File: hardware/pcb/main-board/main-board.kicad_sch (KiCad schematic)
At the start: 44 parts, among them J1 USB-C, J10 CH552G_KEYBOARD_MCU, J11 KEYBOARD_BACKLIGHT_LEDS, J12 SPEAKER_1W_8OHM, J2 BATT_2x18650_PARALLEL, J3 BOOT0_OVERRIDE_JUMPER, J4 SWD_DEBUG, J5 MICROSD, J6 CR2032_HOLDER, J7 U.FL, J8 SMA_EDGE, J9 RA8875_DISPLAY_MODULE, Q1 2N7002, SW1 PWR_KEY, SW2 RESET, U1 MCP73831-2-OT, U10 PAM8403D, U2 IP5306, U3 AMS1117-3.3, U4 AMS1117-3.3, U5 GD32VF103CCT6, U6 W25Q64JVSSIQ, U7 23LC1024, U8 DS3231M, U9 ESP32-C3-MINI-1U, Y1 8MHz

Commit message: hardware: add PCB component placement for the Main Board
Adds main-board.kicad_pcb: every part from the schematic placed within
the 100x80mm board outline (hardware/bom.md's Board 2 spec), on the
correct nets (full ratsnest), courtyard-overlap/shorting/clearance clean
per kicad-cli pcb drc. No copper routing yet -- that's manual follow-on
work in the KiCad GUI (no autorouter available here).

Placement (kicad_gen/build_pcb.py) is computed from each footprint's real
measured courtyard geometry via pcbnew, not guessed -- a first hand-placed
attempt produced 7 courtyard overlaps once real sizes were checked (the
CR2032 holder alone is 27x24mm). Also fixes a footprint-anchor bug found
along the way: schematic instances without an explicit footprint override
were emitting an empty Footprint property, silently blanking out several
real KiCad-library defaults, which in turn exposed three wrong footprint
references (CR2032 holder was pointing at a 9V PP3 clip; two RF connectors
used a nonexistent library name).

Also fixes a schematic-legibility bug: net labels for left-pointing pins
grew back into the component body instead of away from it, and several
component Value fields held long descriptive sentences that collided with
neighboring text -- both cleaned up, with the descriptive notes moved to
README.md instead.

Co-Authored-By: Claude Sonnet 5 <noreply@anthropic.com>
Claude-Session: https://claude.ai/code/session_01Qv22nN2Gzvn3yFBup6Askg
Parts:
- C1, C2, C3: footprint (none) -> Capacitor_SMD:C_0603_1608Metric
- D1, D2: footprint (none) -> LED_SMD:LED_0603_1608Metric
- J5: footprint Connector_Card:Molex_502031-0810_MicroSD -> Connector_Card:microSD_HC_Molex_104031-0811
- J6: footprint Battery:BatteryHolder_MPD_BA9V-1_1x20mm -> Battery:BatteryHolder_MYOUNG_BS-07-A1BJ001_CR2032
- J7: footprint RF_Connector:U.FL_Molex_MCRF_73412-0110 -> Connector_Coaxial:U.FL_Molex_MCRF_73412-0110_Vertical
- Q1: footprint (none) -> Package_TO_SOT_SMD:SOT-23
- R1, R10, R11, R12, R13, R2, R3, R4, R5, R6, R7, R8, R9: footprint (none) -> Resistor_SMD:R_0603_1608Metric
- SW1, SW2: footprint (none) -> Button_Switch_THT:SW_PUSH_6mm_H4.3mm
- U1: footprint (none) -> Package_TO_SOT_SMD:SOT-23-5
- U10: footprint (none) -> Package_SO:SOP-16_3.9x9.9mm_P1.27mm
- U2: footprint (none) -> Package_SO:SOP-8_3.9x4.9mm_P1.27mm
- U3, U4: footprint (none) -> Package_TO_SOT_SMD:SOT-223-3_TabPin2
- U5: footprint (none) -> Package_QFP:LQFP-48_7x7mm_P0.5mm
- U6: footprint (none) -> Package_SO:SOIC-8_5.3x5.3mm_P1.27mm
- U7: footprint (none) -> Package_SO:SOIC-8_3.9x4.9mm_P1.27mm
- U8: footprint (none) -> Package_SO:SOIC-16W_7.5x10.3mm_P1.27mm
- U9: footprint (none) -> RF_Module:ESP32-C3-WROOM-02U
- Y1: footprint (none) -> Crystal:Crystal_SMD_HC49-SD

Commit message: hardware: fix real pin-number bugs found by datasheet verification
Checked all four custom part symbols (23LC1024, GD32VF103CCT6,
ESP32-C3-MINI-1U, IP5306) against their primary-source datasheets.
23LC1024 was already correct. The other three were substantially
wrong, not just unverified:

- GD32VF103CCT6: 35 of 48 pins (14-48) numbered wrong -- two spurious
  power-pin insertions shifted everything after them.
- ESP32-C3-MINI-1U: the symbol numbered its 19 signal pins 1-19
  sequentially; the real 53-pad module has GND/NC scattered through
  that range, so almost nothing lined up.
- IP5306: all 8 pins wrong, plus LED3 and SW (the boost converter's
  inductor node) were missing entirely, and two GND pins were invented
  that don't exist -- the real part's only ground is the PowerPAD.
  Fixing this surfaced a real design gap: no inductor exists anywhere
  in this design, so the boost path can't function yet.

Re-mapped every schematic net/power/no_connect reference to these
three parts to the corrected pin numbers and regenerated the
schematic -- ERC clean (320 warnings, 0 errors, same benign categories
as before).

main-board.kicad_pcb is deliberately left untouched: it was routed
against the old (wrong) netlist, so its net-to-pad assignments on all
three parts are now wrong, not just stale. Documented this plainly in
the PCB README rather than silently leaving a fabrication-unsafe board
looking finished.

Co-Authored-By: Claude Sonnet 5 <noreply@anthropic.com>
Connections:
- net +3V3_MCU: now also U5.24 (VDD_1), U5.36 (VDD_2), U5.48 (VDD_3); no longer U5.15 (VDD_1), U5.26 (VDD_2), U5.38 (VDD_3)
- net +3V3_RF: now also U9.3 (3V3); no longer U9.2 (3V3)
- net +5V: now also U2.8 (VOUT); no longer U2.5 (VOUT)
- net AUDIO_PWM: now also U5.14 (PA4); no longer U5.16 (PA4)
- net AUDIO_SHDN: now also U5.29 (PA8); no longer U5.31 (PA8)
- net BATT_LED1: now also U2.2 (LED1); no longer U2.7 (LED1)
- net BOOT0: now also U5.44 (BOOT0); no longer U5.46 (BOOT0)
- net BOOT1: now also U5.20 (PB2/BOOT1); no longer U5.22 (PB2/BOOT1)
- net DISP_CS: now also U5.25 (PB12); no longer U5.27 (PB12)
- net DISP_RESET: now also U5.38 (PA15); no longer U5.40 (PA15)
- net ESP_EN: now also U9.8 (EN); no longer U9.3 (EN)
- net ESP_IO9: now also U9.23 (IO9/BOOT); no longer U9.13 (IO9/BOOT)
- net GND: now also U2.9 (GND), U5.23 (VSS_1), U5.35 (VSS_2), U5.47 (VSS_3), U9.2 (GND); no longer U2.3 (GND), U2.6 (GND), U5.14 (VSS_1), U5.25 (VSS_2), U5.37 (VSS_3), U9.19 (GND)
- net I2C1_SCL: now also U5.42 (PB6); no longer U5.44 (PB6)
- net I2C1_SDA: now also U5.43 (PB7); no longer U5.45 (PB7)
- net KBD_BACKLIGHT_PWM: now also U5.41 (PB5); no longer U5.43 (PB5)
- net PWR_KEY: now also U2.5 (KEY); no longer U2.4 (KEY)
- net SPI1_MISO: now also U5.16 (PA6); no longer U5.18 (PA6)
- net SPI1_MOSI: now also U5.17 (PA7); no longer U5.19 (PA7)
- net SPI1_SCK: now also U5.15 (PA5); no longer U5.17 (PA5)
- net SPI2_MISO: now also U5.27 (PB14); no longer U5.29 (PB14)
- net SPI2_MOSI: now also U5.28 (PB15); no longer U5.30 (PB15)
- net SPI2_SCK: now also U5.26 (PB13); no longer U5.28 (PB13)
- net SWCLK: now also U5.37 (PA14/SWCLK); no longer U5.39 (PA14/SWCLK)
- net SWDIO: now also U5.34 (PA13/SWDIO); no longer U5.36 (PA13/SWDIO)
- net USART1_RX: now also U5.31 (PA10), U9.31 (U0TXD); no longer U5.33 (PA10), U9.18 (U0TXD)
- net USART1_TX: now also U5.30 (PA9), U9.30 (U0RXD); no longer U5.32 (PA9), U9.17 (U0RXD)
- net USART2_RX: now also U5.40 (PB4); no longer U5.42 (PB4)
- net USART2_TX: now also U5.39 (PB3); no longer U5.41 (PB3)
- net USB_DN: now also U9.26 (IO18/USB_D-); no longer U9.15 (IO18/USB_D-)
- net USB_DP: now also U9.27 (IO19/USB_D+); no longer U9.16 (IO19/USB_D+)
- net VBATT: now also U2.6 (BAT); no longer U2.2 (BAT)
- no-connect marks 31 -> 33

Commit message: hardware: add the IP5306's missing boost inductor
Datasheet verification (previous commit) found the IP5306's SW pin
(the boost converter's switch node) was wired to nothing -- the boost
path (BAT -> VOUT) couldn't function without an inductor there, and
none existed anywhere in this design.

Fixed per the IP5306 datasheet's own "Typical Application Schematic"
(Figure 7): a 1uH inductor (L1) bridges SW to BAT directly, not to
VOUT as an earlier read of this design assumed -- it's shared between
the buck charger and boost discharger. Added the reference circuit's
RC snubber (R14 0.5R + C4 22uF) on the SW node and a VOUT decoupling
cap (C5, simplified from the datasheet's 4-cap bank to one).

Regenerated the schematic (ERC clean) and the PCB from scratch against
the updated netlist: fresh placement (the new parts go in the open
board area below the MCU cluster, since the CR2032 holder's real
courtyard already fills the power-tree column), fresh Freerouting
pass, one net (/USB_DN, unrelated -- same fix as the previous PCB
regeneration) finished by hand. All 87 nets routed, DRC clean except
the pre-existing, already-documented ESP32 placeholder footprint
warning.

Flagged for the next design-review pass: the new SW/inductor path
carries boost-converter current (up to 2.4A) but was auto-routed at
the board's default 0.2mm trace width, which is undersized for it.

Co-Authored-By: Claude Sonnet 5 <noreply@anthropic.com>
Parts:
- added C4: 20pF, Capacitor_SMD:C_0603_1608Metric, symbol Device:C
- added C5: 100nF, Capacitor_SMD:C_0603_1608Metric, symbol Device:C
- added L1: 1uH, Inductor_SMD:L_6.3x6.3_H3, symbol Device:L
- added R14: 1k, Resistor_SMD:R_0603_1608Metric, symbol Device:R
- C1, C2: value 20pF -> 22uF; footprint Capacitor_SMD:C_0603_1608Metric -> Capacitor_SMD:C_0805_2012Metric
- C3: value 100nF -> 20pF
- R11: value 10k -> 4.7k
- R13: value 1k -> 10k
- R5: value 1k -> 0.5R
- R6: value 10k -> 1k
- R9: value 4.7k -> 10k
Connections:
- net +3V3_MCU: now also R11.2, R7.2; no longer R6.2, R9.2
- net +3V3_RF: now also R13.2; no longer R11.2
- net +5V: now also C2.1, R6.1; no longer R5.1
- net AUDIO_IN: now also C5.1, R14.2; no longer C3.1, R13.2
- net AUDIO_PWM: now also R14.1; no longer R13.1
- net BATT_LED1_R: now also R6.2; no longer R5.2
- net BOOT0: now also R8.1; no longer R7.1
- net BOOT1: now also R9.1; no longer R8.1
- net ESP_EN: now also R12.1; no longer R11.1
- net ESP_IO9: now also R13.1; no longer R12.1
- net GND: now also R9.2, C4.2, C5.2; no longer R7.2
- net I2C1_SCL: now also R10.1; no longer R9.1
- net I2C1_SDA: now also R11.1; no longer R10.1
- net NRST: now also R7.1; no longer R6.1
- net OSC_IN: now also C3.1; no longer C1.1
- net OSC_OUT: now also C4.1; no longer C2.1
- net VBATT: now also L1.2
- net IP5306_SW: now reaches U2.7 (SW)
- net IP5306_SW: now also R5.1, L1.1
- new net SNUBBER_MID: C1.1, R5.2
- no-connect marks 33 -> 32

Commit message: hardware: replace the ESP32-C3-MINI-1U placeholder with its real footprint
The datasheet verification pass (two commits back) fixed the schematic
symbol's pin numbers but left the PCB footprint as the same-family
RF_Module:ESP32-C3-WROOM-02U placeholder. Rather than hand-transcribe
a 53-pad castellated land pattern off the datasheet's dimension
drawing -- error-prone, and exactly the kind of mistake this whole
verification effort exists to catch -- vendored the real footprint
from Espressif's official KiCad library (CC-BY-SA 4.0, same terms as
KiCad's own libraries) into a new gridnet_footprints.pretty/, with
build_pcb.py gaining a small local-footprint-library lookup to load
it. Verified before use: 53 distinct pad numbers, pad 49 (GND) present
as the expected 3x3 thermal-via array, matching the datasheet table
the symbol's pins were already checked against.

Regenerated the schematic (ERC clean) and the PCB from scratch:
placement, Freerouting pass, one net (/USB_DN, same unrelated fix as
the last two PCB regenerations) finished by hand. Result: 0 DRC
violations, 0 unconnected items -- the drill_out_of_range warnings
present in every DRC run so far in this project's history are gone,
since they traced entirely to the placeholder's own hole spec.

New finding, not yet addressed: the real footprint has ~34 more GND/NC
pads than the schematic symbol wires, including a 3x3 thermal-pad via
array under pin 49 that isn't stitched to any ground pour. Espressif's
guidance recommends grounding all of them for RF/thermal performance;
flagged in the PCB README as a follow-up, not fixed in this pass.

Co-Authored-By: Claude Sonnet 5 <noreply@anthropic.com>
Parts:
- U9: footprint RF_Module:ESP32-C3-WROOM-02U -> gridnet_footprints:ESP32-C3-MINI-1U

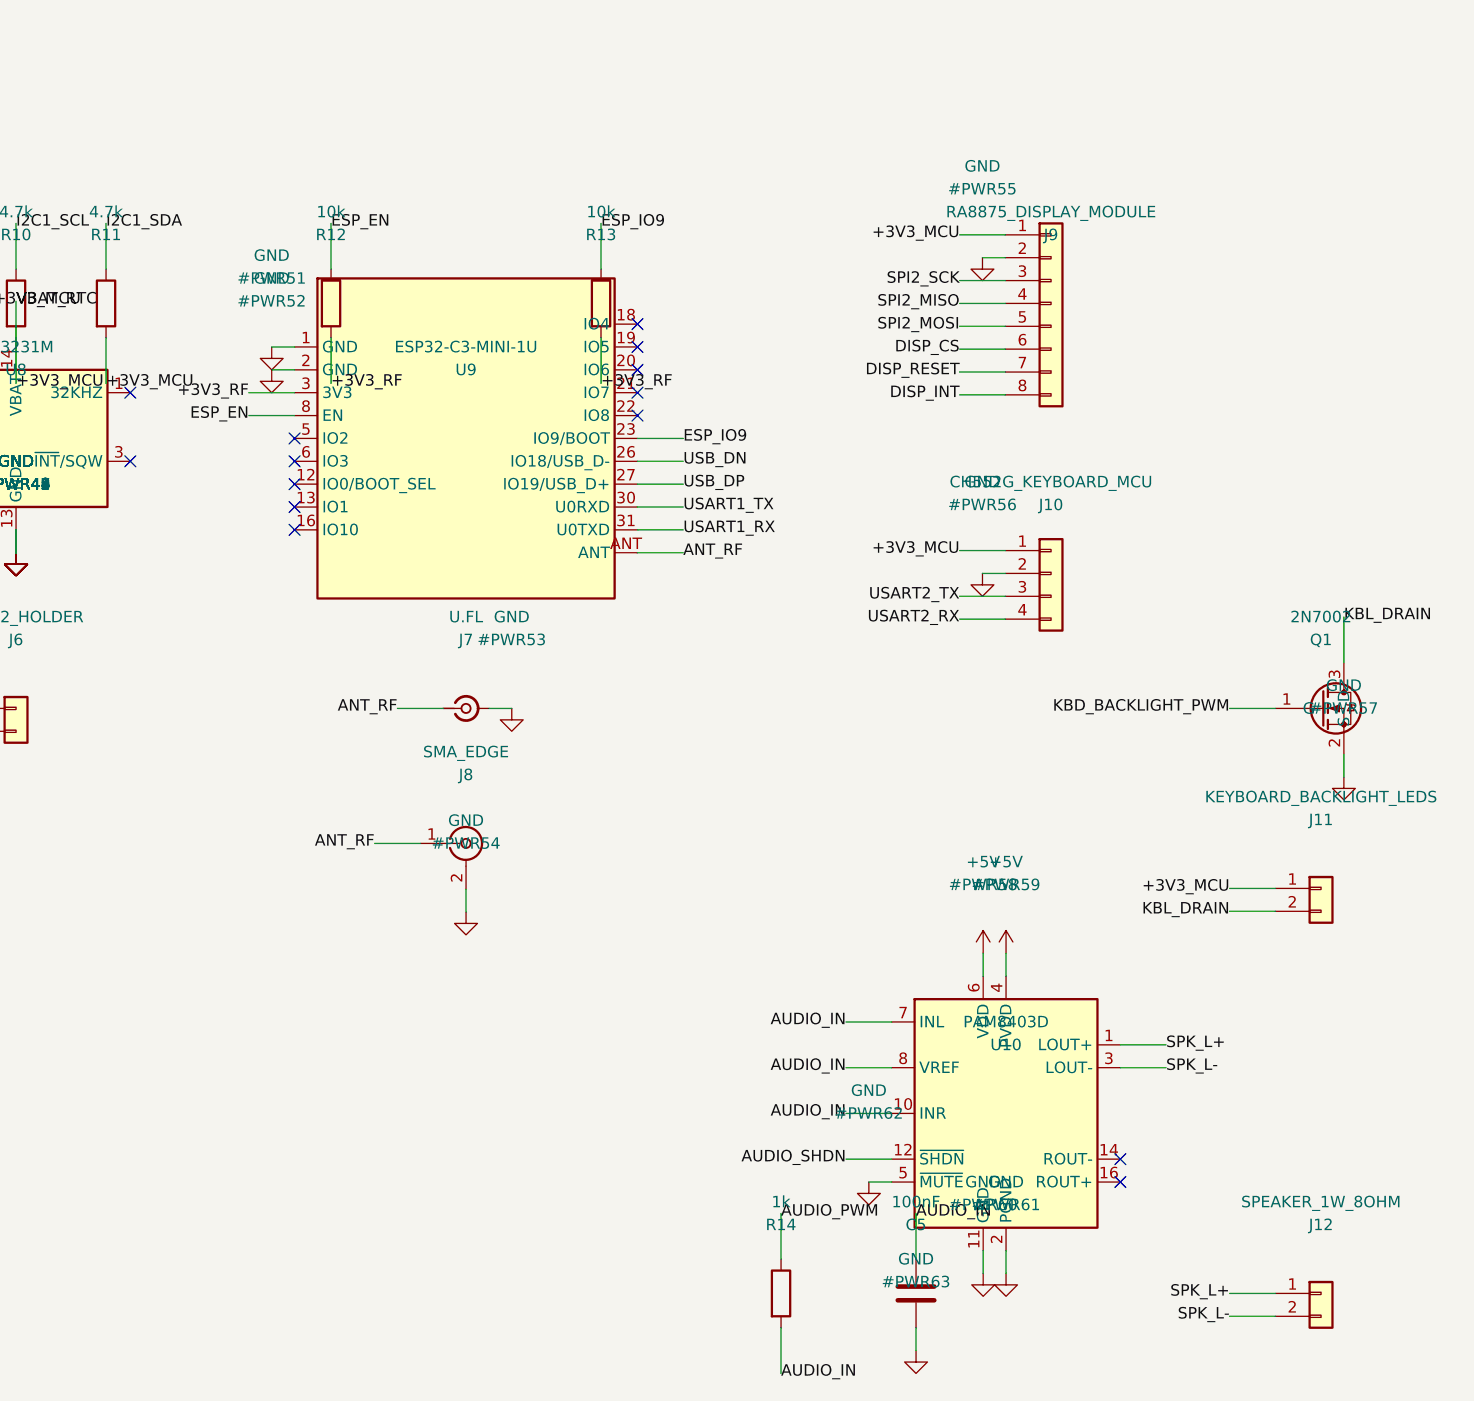
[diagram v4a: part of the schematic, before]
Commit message: hardware: ground the ESP32-C3-MINI-1U's remaining GND/thermal pads
The real footprint swapped in last commit has ~22 GND pin numbers
(30 physical pads once the pin-49 thermal array's 9 copper islands
are counted), but the schematic symbol only drew and wired 2 of them
-- flagged as a follow-up rather than fixed at the time.

Fixed: kicad_gen/build_library.py's ESP32-C3-MINI-1U symbol now draws
every real GND pin from the datasheet's Table 3-1 (1, 2, 11, 14,
36-53), wired to GND in build_schematic.py. Only the module's 14
genuinely NC pads stay undrawn -- there's nothing to connect them to.
Espressif's hardware design guidelines recommend grounding all GND
pads (not just a couple) for this module's RF and thermal performance.

Regenerated schematic (ERC clean) and PCB from scratch: fresh
placement, fresh Freerouting pass. Result: all 192 nets auto-routed
with nothing left to finish by hand -- the first PCB regeneration in
this board's history where Freerouting didn't get stuck on anything.
0 DRC violations, 0 unconnected items, all 30 of U9's GND pads
confirmed on the GND net.

Not done here: an actual copper ground pour/zone stitched to the
thermal pad via array. The pads are now electrically grounded via
ordinary routed traces, which satisfies connectivity but not the full
thermal-performance intent of Espressif's guidance -- left as a
separate PCB-editor task.

Co-Authored-By: Claude Sonnet 5 <noreply@anthropic.com>
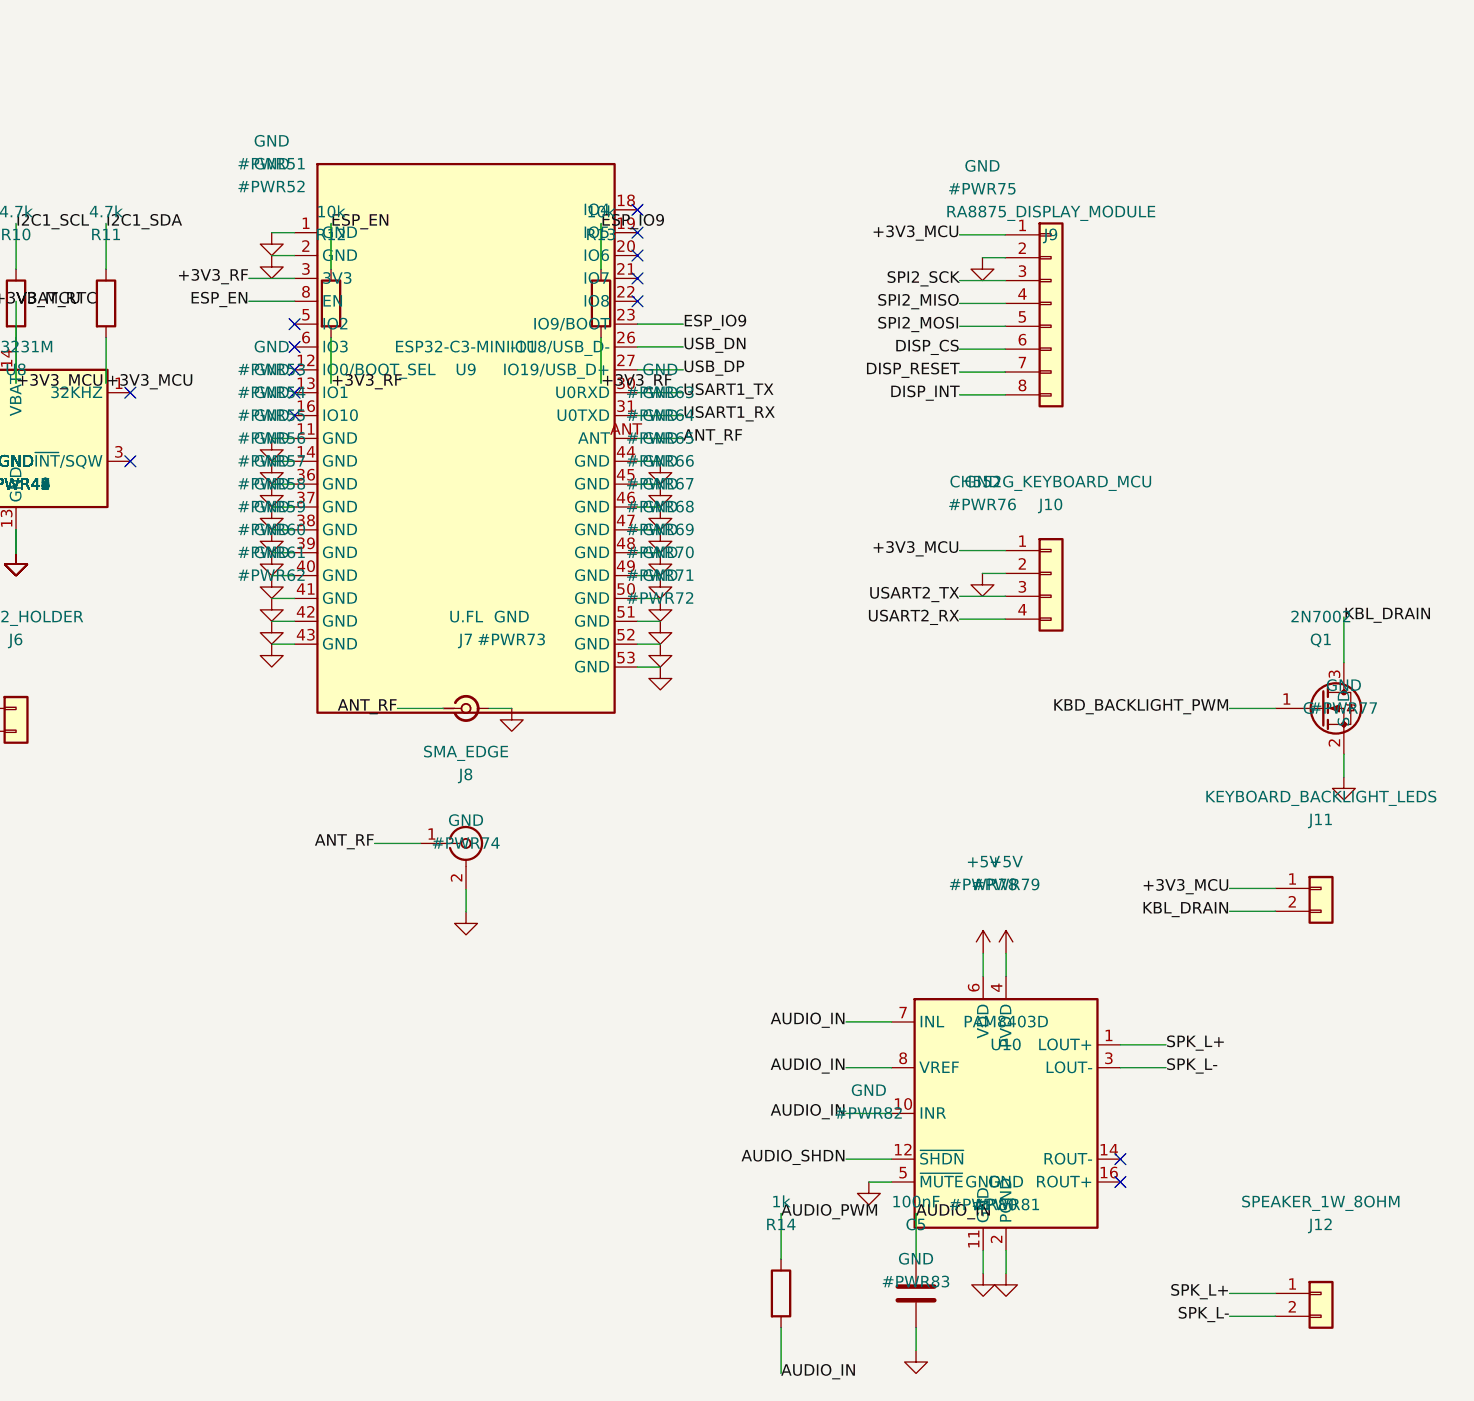
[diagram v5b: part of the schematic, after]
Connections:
- net GND: now also U9.11 (GND), U9.14 (GND), U9.36 (GND), U9.37 (GND), U9.38 (GND), U9.39 (GND), U9.40 (GND), U9.41 (GND), U9.42 (GND), U9.43 (GND), U9.44 (GND), U9.45 (GND), U9.46 (GND), U9.47 (GND), U9.48 (GND), U9.49 (GND), U9.50 (GND), U9.51 (GND), U9.52 (GND), U9.53 (GND)
